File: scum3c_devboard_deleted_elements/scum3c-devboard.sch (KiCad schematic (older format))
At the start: 8 parts, among them U9AB1 MPU-9250

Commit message: routed traces
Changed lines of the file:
@@
 Text Label 4450 3650 2    50   ~ 0
 3WB_DATA
-$Comp
-L Connector_Generic:Conn_01x09 JB1
-U 1 1 5F804045
-P 4650 3650
-F 0 "JB1" H 4730 3692 50  0000 L CNN
-F 1 "Conn_01x09" H 4730 3601 50  0000 L CNN
-F 2 "Connector_PinHeader_1.27mm:PinHeader_1x09_P1.27mm_Vertical" H 4650 3650 50  0001 C CNN
-F 3 "~" H 4650 3650 50  0001 C CNN
-	1    4650 3650
-	1    0    0    -1
-$EndComp
 Text Label 4400 4500 2    50   ~ 0
 GPIO0
@@
 	1    0    0    -1
 $EndComp
+$Comp
+L Connector_Generic:Conn_01x09 JB1
+U 1 1 5F804045
+P 4650 3650
+F 0 "JB1" H 4730 3692 50  0000 L CNN
+F 1 "Conn_01x09" H 4730 3601 50  0000 L CNN
+F 2 "Connector_PinHeader_1.27mm:PinHeader_1x09_P1.27mm_Vertical" H 4650 3650 50  0001 C CNN
+F 3 "~" H 4650 3650 50  0001 C CNN
+	1    4650 3650
+	1    0    0    -1
+$EndComp
+$Comp
+L draft1library:+VDDD #PWR?
+U 1 1 5FCBDE12
+P 4450 3550
+F 0 "#PWR?" H 4450 3400 50  0001 C CNN
+F 1 "+VDDD" H 4465 3723 50  0000 C CNN
+F 2 "" H 4450 3550 50  0001 C CNN
+F 3 "" H 4450 3550 50  0001 C CNN
+	1    4450 3550
+	0    -1   -1   0
+$EndComp
 $EndSCHEMATC

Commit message: added ADC pins
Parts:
- removed JB1: Conn_01x09, Connector_PinHeader_1.27mm:PinHeader_1x09_P1.27mm_Vertical, symbol Connector_Generic:Conn_01x09
- added JB1: Conn_01x11, Connector_PinHeader_1.27mm:PinHeader_1x11_P1.27mm_Vertical, symbol Connector_Generic:Conn_01x11
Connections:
- net labels added: SENSOR_EXT_IN, SENSOR_LDO_OUTPUT
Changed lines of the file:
@@
 AR Path="/5F7B958D" Ref="#PWR0109"  Part="1"
 F 0 "#PWR0109" H 4450 3200 50  0001 C CNN
-F 1 "+VBAT" V 4450 3600 50  0000 C CNN
+F 1 "+VBAT" V 4450 3650 50  0000 C CNN
 F 2 "" H 4450 3350 50  0001 C CNN
 F 3 "" H 4450 3350 50  0001 C CNN
@@
 	0    -1   -1   0
 $EndComp
-Text Label 9400 3250 0    50   ~ 0
+Text Label 9400 2350 0    50   ~ 0
 BOOT_SOURCE_SEL
 Text Label 8550 2950 2    50   ~ 0
@@
 	0    -1   -1   0
 $EndComp
+Text Label 4450 4150 2    50   ~ 0
+RsRx
+Text Label 4450 4250 2    50   ~ 0
+RsTx
+Text Label 4450 4050 2    50   ~ 0
+3WB_CLK
 Text Label 4450 3950 2    50   ~ 0
-RsRx
-Text Label 4450 4050 2    50   ~ 0
-RsTx
+3WB_ENB
 Text Label 4450 3850 2    50   ~ 0
-3WB_CLK
-Text Label 4450 3750 2    50   ~ 0
-3WB_ENB
-Text Label 4450 3650 2    50   ~ 0
 3WB_DATA
 Text Label 4400 4500 2    50   ~ 0
@@
 F13 "RsTx" B L 8550 3050 50
 F14 "RsRx" B L 8550 2950 50
-F15 "BOOT_SOURCE_SEL" B R 9400 3250 50
+F15 "BOOT_SOURCE_SEL" B R 9400 2350 50
+F16 "SENSOR_EXT_IN" B R 9400 2500 50
+F17 "SENSOR_LDO_OUTPUT" B R 9400 2650 50
 $EndSheet
 $Comp
@@
 $EndComp
 $Comp
-L Connector_Generic:Conn_01x09 JB1
-U 1 1 5F804045
-P 4650 3650
-F 0 "JB1" H 4730 3692 50  0000 L CNN
-F 1 "Conn_01x09" H 4730 3601 50  0000 L CNN
-F 2 "Connector_PinHeader_1.27mm:PinHeader_1x09_P1.27mm_Vertical" H 4650 3650 50  0001 C CNN
-F 3 "~" H 4650 3650 50  0001 C CNN
-	1    4650 3650
-	1    0    0    -1
-$EndComp
-$Comp
-L draft1library:+VDDD #PWR?
+L draft1library:+VDDD #PWR0111
 U 1 1 5FCBDE12
 P 4450 3550
-F 0 "#PWR?" H 4450 3400 50  0001 C CNN
-F 1 "+VDDD" H 4465 3723 50  0000 C CNN
+F 0 "#PWR0111" H 4450 3400 50  0001 C CNN
+F 1 "+VDDD" V 4450 3850 50  0000 C CNN
 F 2 "" H 4450 3550 50  0001 C CNN
 F 3 "" H 4450 3550 50  0001 C CNN
@@
 	0    -1   -1   0
 $EndComp
+Text Label 9400 2500 0    50   ~ 0
+SENSOR_EXT_IN
+Text Label 9400 2650 0    50   ~ 0
+SENSOR_LDO_OUTPUT
+$Comp
+L Connector_Generic:Conn_01x11 JB1
+U 1 1 5FCC0A7F
+P 4650 3750
+F 0 "JB1" H 4730 3792 50  0000 L CNN
+F 1 "Conn_01x11" H 4730 3701 50  0000 L CNN
+F 2 "Connector_PinHeader_1.27mm:PinHeader_1x11_P1.27mm_Vertical" H 4650 3750 50  0001 C CNN
+F 3 "~" H 4650 3750 50  0001 C CNN
+	1    4650 3750
+	1    0    0    -1
+$EndComp
+Text Label 4450 3650 2    50   ~ 0
+SENSOR_EXT_IN
+Text Label 4450 3750 2    50   ~ 0
+SENSOR_LDO_OUTPUT
 $EndSCHEMATC

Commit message: deleted zener diode
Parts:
- removed Z1: DDZ9678-7, SamacSys_Parts:SOD3716X135N, symbol SamacSys_Parts:DDZ9678-7
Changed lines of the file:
@@
-	1    0    0    -1
-$EndComp
-$Comp
-L SamacSys_Parts:DDZ9678-7 Z1
-U 1 1 5F7B30CA
-P 4900 6550
-F 0 "Z1" V 5246 6422 50  0000 R CNN
-F 1 "DDZ9678-7" V 5155 6422 50  0000 R CNN
-F 2 "SamacSys_Parts:SOD3716X135N" H 5300 6700 50  0001 L CNN
-F 3 "https://www.mouser.com/datasheet/2/115/ds30410-30695.pdf" H 5300 6600 50  0001 L CNN
-F 4 "Diode Zener 1.8V 5% 500mW 2Pin SOD123" H 5300 6500 50  0001 L CNN "Description"
-F 5 "1.35" H 5300 6400 50  0001 L CNN "Height"
-F 6 "Diodes Inc." H 5300 6300 50  0001 L CNN "Manufacturer_Name"
-F 7 "DDZ9678-7" H 5300 6200 50  0001 L CNN "Manufacturer_Part_Number"
-F 8 "DDZ9678-7" H 5300 6100 50  0001 L CNN "Arrow Part Number"
-F 9 "https://www.arrow.com/en/products/ddz9678-7/diodes-incorporated" H 5300 6000 50  0001 L CNN "Arrow Price/Stock"
-F 10 "621-DDZ9678-7" H 5300 5900 50  0001 L CNN "Mouser Part Number"
-F 11 "https://www.mouser.co.uk/ProductDetail/Diodes-Incorporated/DDZ9678-7?qs=ptj1V1atRAp2rXEOTrnLaA%3D%3D" H 5300 5800 50  0001 L CNN "Mouser Price/Stock"
-	1    4900 6550
-	0    1    1    0
-$EndComp
-$Comp
-L power:GND #PWR0122
-U 1 1 5F7B8192
-P 4900 7150
-F 0 "#PWR0122" H 4900 6900 50  0001 C CNN
-F 1 "GND" H 4905 6977 50  0000 C CNN
-F 2 "" H 4900 7150 50  0001 C CNN
-F 3 "" H 4900 7150 50  0001 C CNN
-	1    4900 7150
-	1    0    0    -1
-$EndComp
-$Comp
-L draft1library:+VBAT #PWR0123
-U 1 1 5F7BC62D
-P 4900 6550
-F 0 "#PWR0123" H 4900 6400 50  0001 C CNN
-F 1 "+VBAT" H 4915 6723 50  0000 C CNN
-F 2 "" H 4900 6550 50  0001 C CNN
-F 3 "" H 4900 6550 50  0001 C CNN
-	1    4900 6550
 	1    0    0    -1
 $EndComp

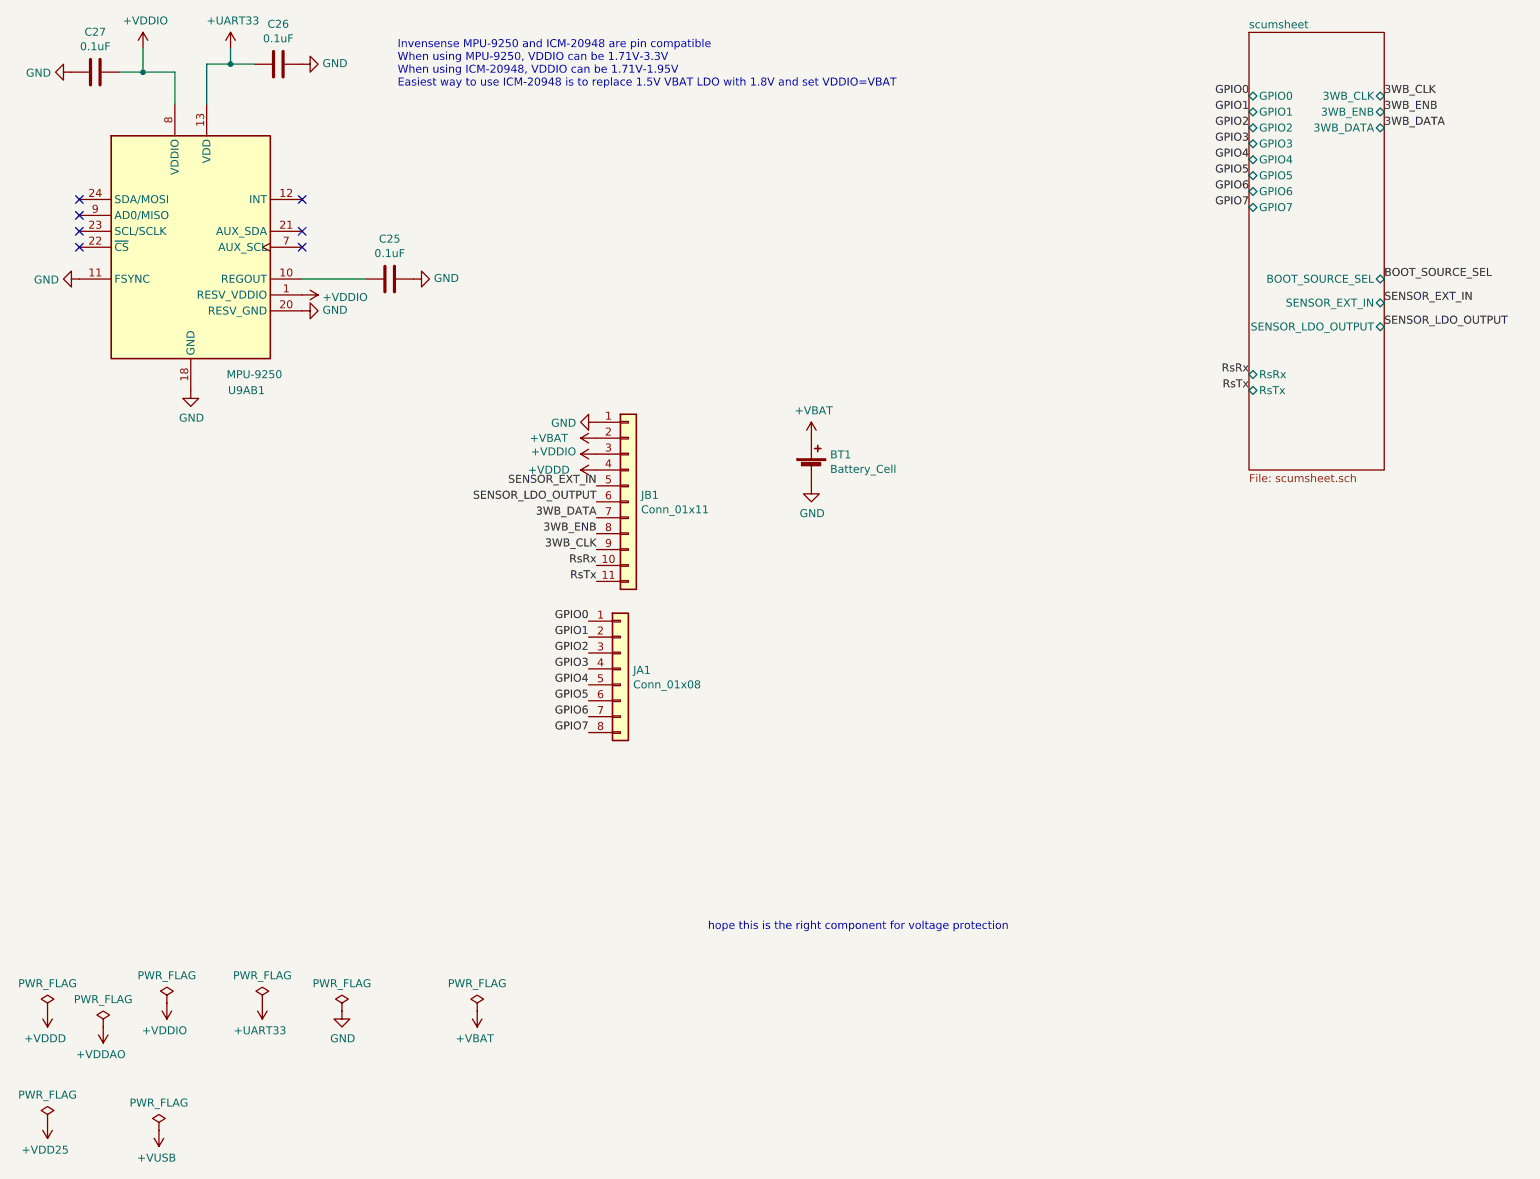
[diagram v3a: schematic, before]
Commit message: added gpio 8 9 10 and gnd pins
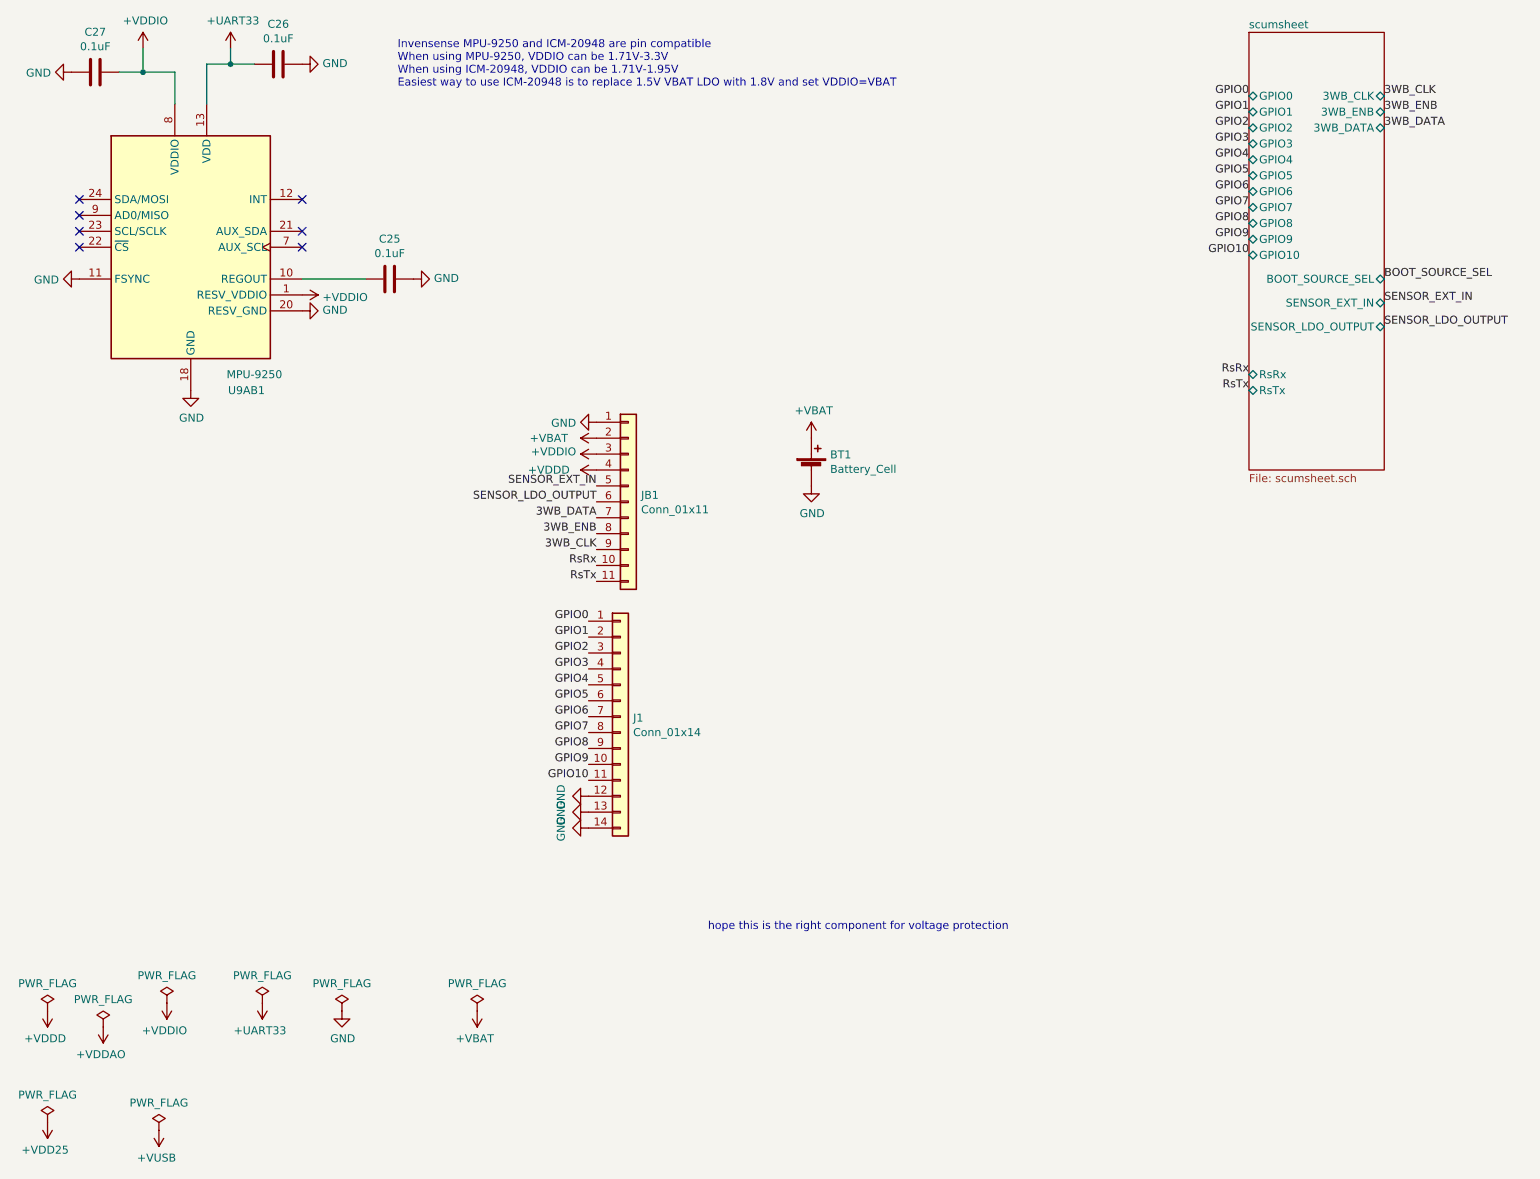
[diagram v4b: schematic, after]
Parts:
- removed JA1: Conn_01x08, Connector_PinHeader_1.27mm:PinHeader_1x08_P1.27mm_Vertical, symbol Connector_Generic:Conn_01x08
- added J1: Conn_01x14, Connector_PinHeader_1.27mm:PinHeader_1x14_P1.27mm_Vertical, symbol Connector_Generic:Conn_01x14
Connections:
- net GND: now also J1.12 (Pin_12), J1.13 (Pin_13), J1.14 (Pin_14)
- net GPIO0: now also J1.1 (Pin_1)
- net GPIO1: now also J1.2 (Pin_2)
- net GPIO2: now also J1.3 (Pin_3)
- net GPIO3: now also J1.4 (Pin_4)
- net GPIO4: now also J1.5 (Pin_5)
- net GPIO5: now also J1.6 (Pin_6)
- net GPIO6: now also J1.7 (Pin_7)
- net GPIO7: now also J1.8 (Pin_8)
- new net GPIO10: J1.11 (Pin_11)
- new net GPIO8: J1.9 (Pin_9)
- new net GPIO9: J1.10 (Pin_10)
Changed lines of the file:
@@
 F16 "SENSOR_EXT_IN" B R 9400 2500 50
 F17 "SENSOR_LDO_OUTPUT" B R 9400 2650 50
+F18 "GPIO8" B L 8550 2000 50
+F19 "GPIO9" B L 8550 2100 50
+F20 "GPIO10" B L 8550 2200 50
 $EndSheet
-$Comp
-L Connector_Generic:Conn_01x08 JA1
-U 1 1 5FCC5985
-P 4600 4800
-F 0 "JA1" H 4680 4792 50  0000 L CNN
-F 1 "Conn_01x08" H 4680 4701 50  0000 L CNN
-F 2 "Connector_PinHeader_1.27mm:PinHeader_1x08_P1.27mm_Vertical" H 4600 4800 50  0001 C CNN
-F 3 "~" H 4600 4800 50  0001 C CNN
-	1    4600 4800
-	1    0    0    -1
-$EndComp
 $Comp
 L draft1library:+VDDD #PWR0111
@@
 Text Label 4450 3750 2    50   ~ 0
 SENSOR_LDO_OUTPUT
+Text Label 8550 2000 2    50   ~ 0
+GPIO8
+Text Label 8550 2100 2    50   ~ 0
+GPIO9
+Text Label 8550 2200 2    50   ~ 0
+GPIO10
+Text Label 4400 5300 2    50   ~ 0
+GPIO8
+Text Label 4400 5400 2    50   ~ 0
+GPIO9
+Text Label 4400 5500 2    50   ~ 0
+GPIO10
+$Comp
+L Connector_Generic:Conn_01x14 J1
+U 1 1 5FCBF099
+P 4600 5100
+F 0 "J1" H 4680 5092 50  0000 L CNN
+F 1 "Conn_01x14" H 4680 5001 50  0000 L CNN
+F 2 "Connector_PinHeader_1.27mm:PinHeader_1x14_P1.27mm_Vertical" H 4600 5100 50  0001 C CNN
+F 3 "~" H 4600 5100 50  0001 C CNN
+	1    4600 5100
+	1    0    0    -1
+$EndComp
+$Comp
+L power:GND #PWR0112
+U 1 1 5FCC0D5E
+P 4400 5600
+AR Path="/5FCC0D5E" Ref="#PWR0112"  Part="1"
+AR Path="/5F3B0B28/5FCC0D5E" Ref="#PWR?"  Part="1"
+F 0 "#PWR0112" H 4400 5350 50  0001 C CNN
+F 1 "GND" H 4405 5427 50  0000 C CNN
+F 2 "" H 4400 5600 50  0001 C CNN
+F 3 "" H 4400 5600 50  0001 C CNN
+	1    4400 5600
+	0    1    1    0
+$EndComp
+$Comp
+L power:GND #PWR0122
+U 1 1 5FCC1320
+P 4400 5700
+AR Path="/5FCC1320" Ref="#PWR0122"  Part="1"
+AR Path="/5F3B0B28/5FCC1320" Ref="#PWR?"  Part="1"
+F 0 "#PWR0122" H 4400 5450 50  0001 C CNN
+F 1 "GND" H 4405 5527 50  0000 C CNN
+F 2 "" H 4400 5700 50  0001 C CNN
+F 3 "" H 4400 5700 50  0001 C CNN
+	1    4400 5700
+	0    1    1    0
+$EndComp
+$Comp
+L power:GND #PWR0123
+U 1 1 5FCC1462
+P 4400 5800
+AR Path="/5FCC1462" Ref="#PWR0123"  Part="1"
+AR Path="/5F3B0B28/5FCC1462" Ref="#PWR?"  Part="1"
+F 0 "#PWR0123" H 4400 5550 50  0001 C CNN
+F 1 "GND" H 4405 5627 50  0000 C CNN
+F 2 "" H 4400 5800 50  0001 C CNN
+F 3 "" H 4400 5800 50  0001 C CNN
+	1    4400 5800
+	0    1    1    0
+$EndComp
 $EndSCHEMATC

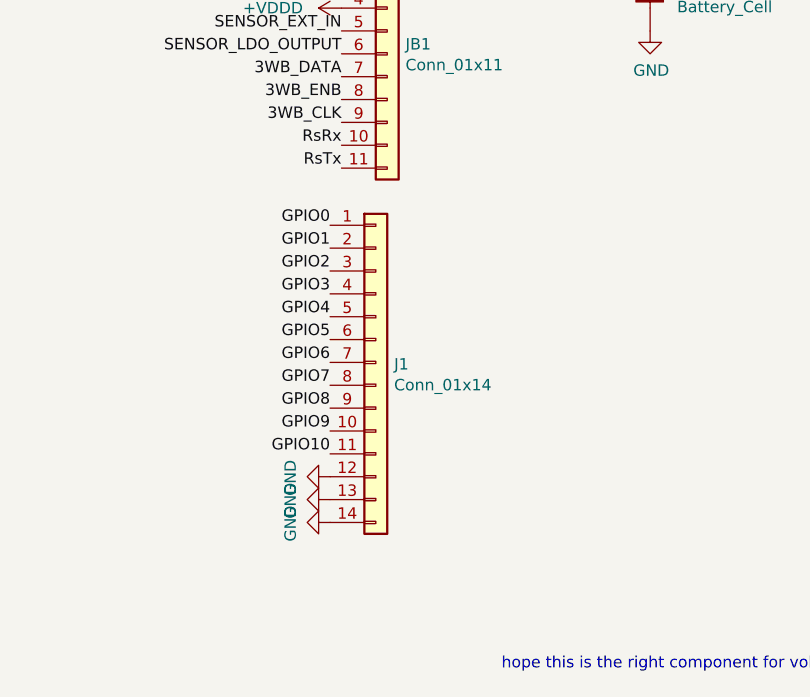
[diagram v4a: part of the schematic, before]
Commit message: flipped around gpio headers
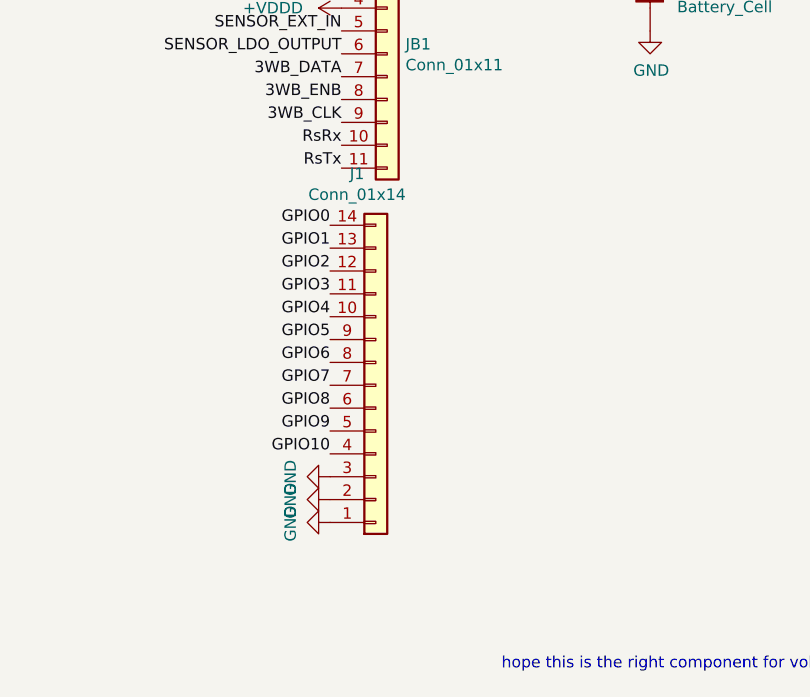
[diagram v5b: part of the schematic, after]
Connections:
- net GND: now also J1.1 (Pin_1), J1.2 (Pin_2), J1.3 (Pin_3); no longer J1.12 (Pin_12), J1.13 (Pin_13), J1.14 (Pin_14)
- net GPIO0: now also J1.14 (Pin_14); no longer J1.1 (Pin_1)
- net GPIO1: now also J1.13 (Pin_13); no longer J1.2 (Pin_2)
- net GPIO10: now also J1.4 (Pin_4); no longer J1.11 (Pin_11)
- net GPIO2: now also J1.12 (Pin_12); no longer J1.3 (Pin_3)
- net GPIO3: now also J1.11 (Pin_11); no longer J1.4 (Pin_4)
- net GPIO4: now also J1.10 (Pin_10); no longer J1.5 (Pin_5)
- net GPIO5: now also J1.9 (Pin_9); no longer J1.6 (Pin_6)
- net GPIO6: now also J1.8 (Pin_8); no longer J1.7 (Pin_7)
- net GPIO7: now also J1.7 (Pin_7); no longer J1.8 (Pin_8)
- net GPIO8: now also J1.6 (Pin_6); no longer J1.9 (Pin_9)
- net GPIO9: now also J1.5 (Pin_5); no longer J1.10 (Pin_10)
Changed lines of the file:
@@
 L Connector_Generic:Conn_01x14 J1
 U 1 1 5FCBF099
-P 4600 5100
-F 0 "J1" H 4680 5092 50  0000 L CNN
-F 1 "Conn_01x14" H 4680 5001 50  0000 L CNN
-F 2 "Connector_PinHeader_1.27mm:PinHeader_1x14_P1.27mm_Vertical" H 4600 5100 50  0001 C CNN
-F 3 "~" H 4600 5100 50  0001 C CNN
-	1    4600 5100
-	1    0    0    -1
+P 4600 5200
+F 0 "J1" H 4518 4275 50  0000 C CNN
+F 1 "Conn_01x14" H 4518 4366 50  0000 C CNN
+F 2 "Connector_PinHeader_1.27mm:PinHeader_1x14_P1.27mm_Vertical" H 4600 5200 50  0001 C CNN
+F 3 "~" H 4600 5200 50  0001 C CNN
+	1    4600 5200
+	1    0    0    1
 $EndComp
 $Comp

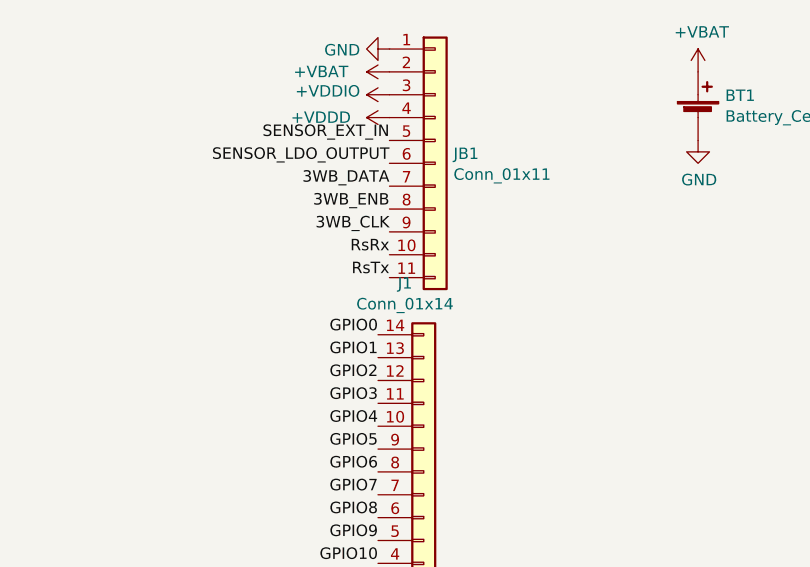
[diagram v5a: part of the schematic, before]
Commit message: "J1"->"JA1"
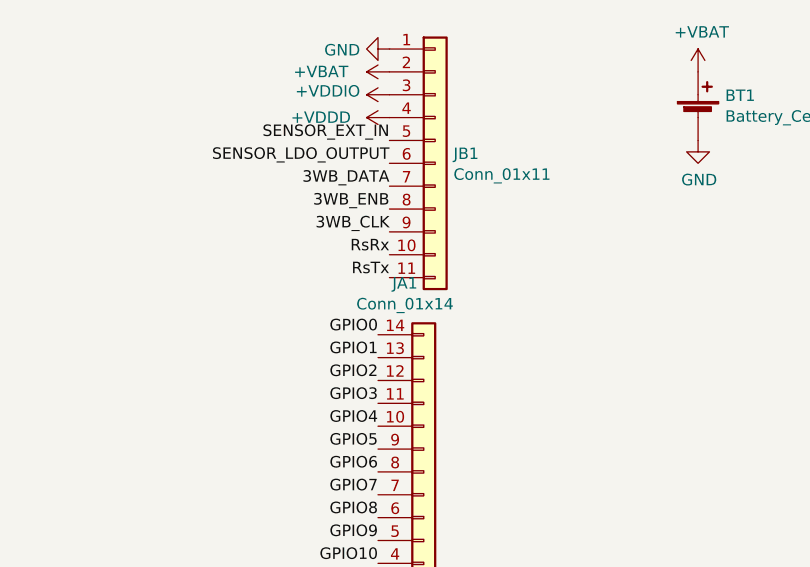
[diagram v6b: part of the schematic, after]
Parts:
- renumbered J1 to JA1
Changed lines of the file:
@@
 GPIO10
 $Comp
-L Connector_Generic:Conn_01x14 J1
+L Connector_Generic:Conn_01x14 JA1
 U 1 1 5FCBF099
 P 4600 5200
-F 0 "J1" H 4518 4275 50  0000 C CNN
+F 0 "JA1" H 4518 4275 50  0000 C CNN
 F 1 "Conn_01x14" H 4518 4366 50  0000 C CNN
 F 2 "Connector_PinHeader_1.27mm:PinHeader_1x14_P1.27mm_Vertical" H 4600 5200 50  0001 C CNN
